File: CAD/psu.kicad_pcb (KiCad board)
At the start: 2 copper layers, 85.5 x 107 mm, 33 parts, among them J2 Vout conn, J3 OLED Pins, J4 GND/-, Q1 tip35c, Q2 BD139, Q3 BC184C, Q4 BC547, T1 220/24, U1 TL431LP, U2 LM317_TO-220, U3 DS18B20

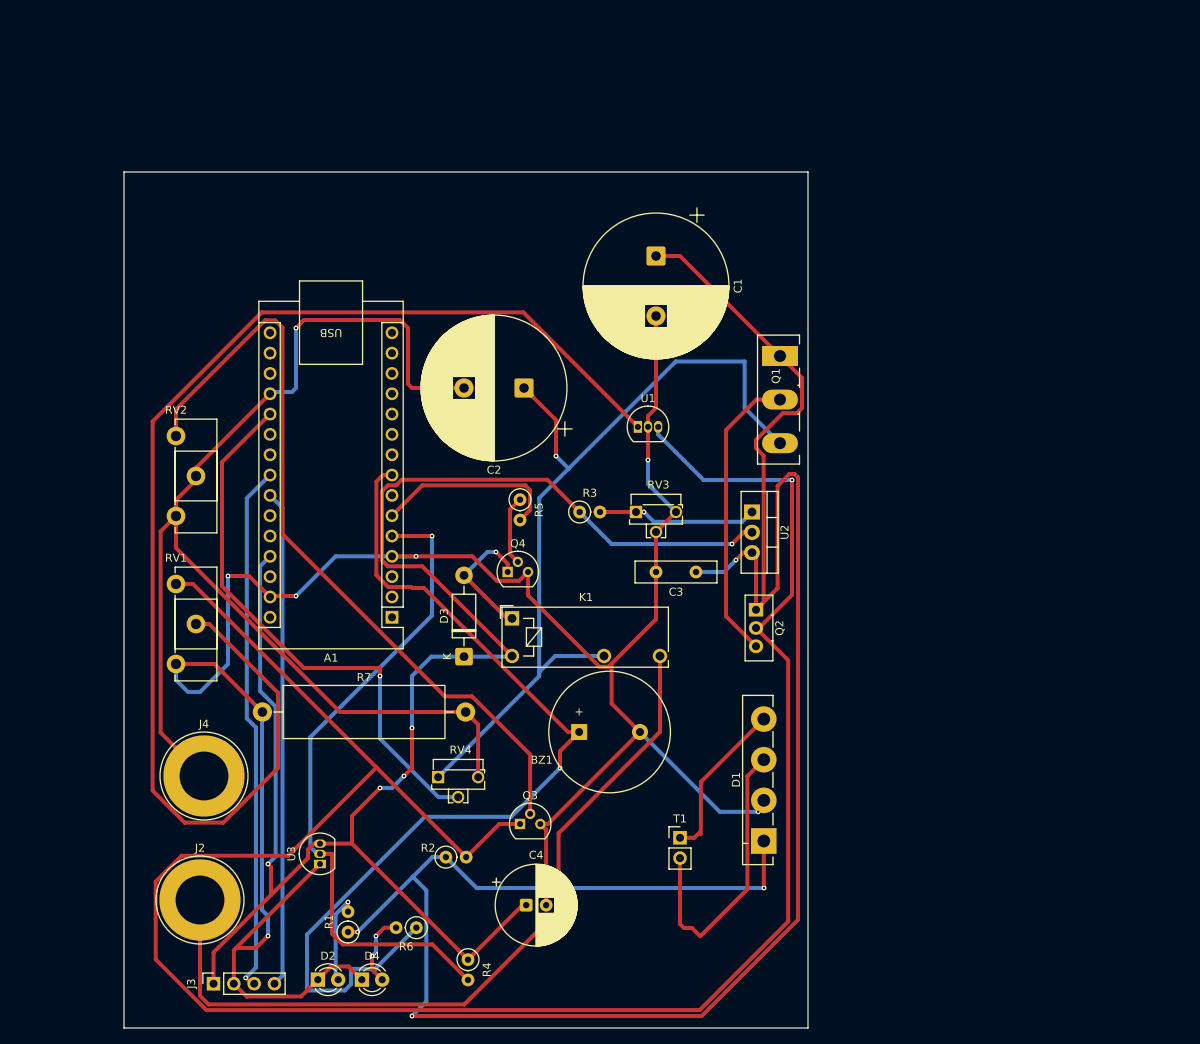
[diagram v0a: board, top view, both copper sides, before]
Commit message: PCB and SCH finished and PDF for self manufacturing finished
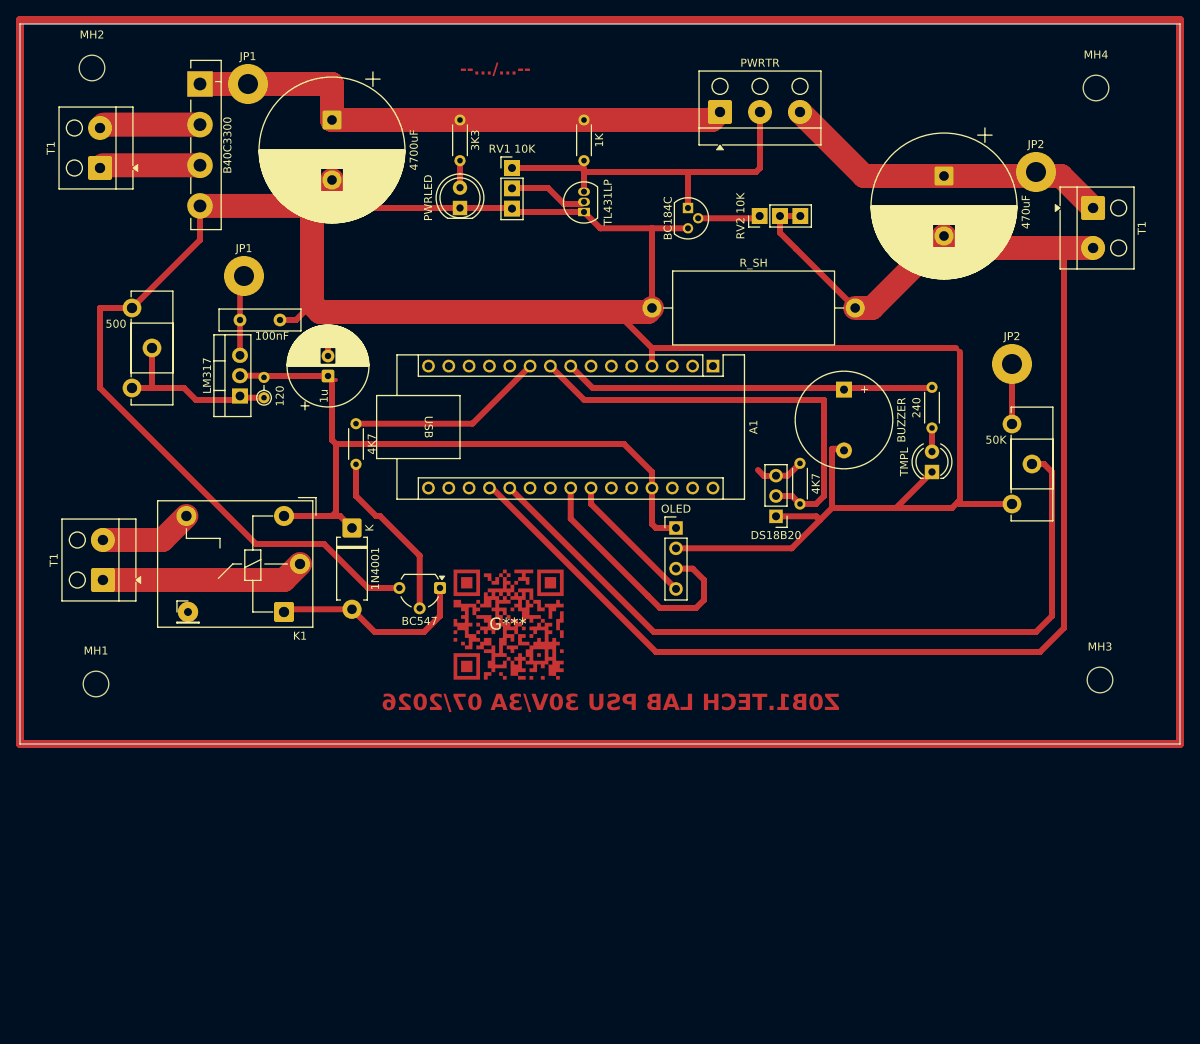
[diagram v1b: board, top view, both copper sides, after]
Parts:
- removed BZ1: T_Buzzer, Buzzer_Beeper:Buzzer_15x7.5RM7.6
- removed C1: 4700uF 40V, Capacitor_THT:CP_Radial_D18.0mm_P7.50mm
- removed C2: 470uF 40v, Capacitor_THT:CP_Radial_D18.0mm_P7.50mm
- removed C3: 100n, Capacitor_THT:C_Disc_D10.0mm_W2.5mm_P5.00mm
- removed C4: 1u, Capacitor_THT:CP_Radial_D10.0mm_P2.50mm
- removed D1: ABS2, Diode_THT:Diode_Bridge_Vishay_GBL
- removed D2: LED, LED_THT:LED_D3.0mm
- removed D3: D, Diode_THT:D_DO-41_SOD81_P10.16mm_Horizontal
- removed D4: T_LED, LED_THT:LED_D3.0mm
- removed J2: Vout conn, Connector:Banana_Jack_1Pin
- removed J3: OLED Pins, Connector_PinSocket_2.54mm:PinSocket_1x04_P2.54mm_Vertical
- removed J4: GND/-, Connector:Banana_Jack_1Pin
- removed Q1: tip35c, Package_TO_SOT_THT:TO-247-3_Vertical
- removed Q2: BD139, Package_TO_SOT_THT:TO-126-3_Vertical
- removed Q3: BC184C, Package_TO_SOT_THT:TO-92
- removed Q4: BC547, Package_TO_SOT_THT:TO-92
- removed R1: 3k3, Resistor_THT:R_Axial_DIN0207_L6.3mm_D2.5mm_P2.54mm_Vertical
- removed R2: 1k, Resistor_THT:R_Axial_DIN0207_L6.3mm_D2.5mm_P2.54mm_Vertical
- removed R3: 120, Resistor_THT:R_Axial_DIN0207_L6.3mm_D2.5mm_P2.54mm_Vertical
- removed R4, R5: 4k7, Resistor_THT:R_Axial_DIN0207_L6.3mm_D2.5mm_P2.54mm_Vertical
- removed R6: 220, Resistor_THT:R_Axial_DIN0207_L6.3mm_D2.5mm_P2.54mm_Vertical
- removed R7: 0R5/5W, Resistor_THT:R_Axial_Power_L20.0mm_W6.4mm_P25.40mm
- removed RV1, RV2: 10k, Potentiometer_THT:Potentiometer_ACP_CA14-H2,5_Horizontal
- removed RV3: 500, Potentiometer_THT:Potentiometer_Runtron_RM-063_Horizontal
- removed RV4: 50K, Potentiometer_THT:Potentiometer_Runtron_RM-063_Horizontal
- removed the T1 at (103.0, 116.7)
- removed U1: TL431LP, Package_TO_SOT_THT:TO-92_Inline
- removed U2: LM317_TO-220, Package_TO_SOT_THT:TO-220-3_Vertical
- removed U3: DS18B20, Package_TO_SOT_THT:TO-92_Inline
- added 100nF: C_Disc_D10.0mm_W2.5mm_P5.00mm, Capacitor_THT:C_Disc_D10.0mm_W2.5mm_P5.00mm, F.Cu at (48.0, 52.0)
- added 120: R_Axial_DIN0204_L3.6mm_D1.6mm_P2.54mm_Vertical, Resistor_THT:R_Axial_DIN0204_L3.6mm_D1.6mm_P2.54mm_Vertical, F.Cu at (51.0, 61.7)
- added 1K: R_Axial_DIN0204_L3.6mm_D1.6mm_P5.08mm_Horizontal, Resistor_THT:R_Axial_DIN0204_L3.6mm_D1.6mm_P5.08mm_Horizontal, F.Cu at (91.0, 27.0)
- added 1N4001: D_DO-15_P10.16mm_Horizontal, Diode_THT:D_DO-15_P10.16mm_Horizontal, F.Cu at (62.0, 78.0)
- added 1u: CP_Radial_D10.0mm_P2.50mm, Capacitor_THT:CP_Radial_D10.0mm_P2.50mm, F.Cu at (59.0, 59.0)
- added 240: R_Axial_DIN0204_L3.6mm_D1.6mm_P5.08mm_Horizontal, Resistor_THT:R_Axial_DIN0204_L3.6mm_D1.6mm_P5.08mm_Horizontal, F.Cu at (134.5, 65.5)
- added 3K3: R_Axial_DIN0204_L3.6mm_D1.6mm_P5.08mm_Horizontal, Resistor_THT:R_Axial_DIN0204_L3.6mm_D1.6mm_P5.08mm_Horizontal, F.Cu at (75.5, 27.0)
- added 4700uF: CP_Radial_D18.0mm_P7.50mm, Capacitor_THT:CP_Radial_D18.0mm_P7.50mm, F.Cu at (59.5, 27.0)
- added 470uF: CP_Radial_D18.0mm_P7.50mm, Capacitor_THT:CP_Radial_D18.0mm_P7.50mm, F.Cu at (136.0, 34.0)
- added 4K7: R_Axial_DIN0204_L3.6mm_D1.6mm_P5.08mm_Horizontal, Resistor_THT:R_Axial_DIN0204_L3.6mm_D1.6mm_P5.08mm_Horizontal, F.Cu at (62.5, 70.0)
- added 4K7: R_Axial_DIN0204_L3.6mm_D1.6mm_P5.08mm_Horizontal, Resistor_THT:R_Axial_DIN0204_L3.6mm_D1.6mm_P5.08mm_Horizontal, F.Cu at (118.0, 75.0)
- added 500: Potentiometer_ACP_CA14-H2,5_Horizontal, Potentiometer_THT:Potentiometer_ACP_CA14-H2,5_Horizontal, F.Cu at (34.5, 50.5)
- added 50K: Potentiometer_ACP_CA14-H2,5_Horizontal, Potentiometer_THT:Potentiometer_ACP_CA14-H2,5_Horizontal, F.Cu at (144.5, 65.0)
- added B40C3300: Diode_Bridge_Vishay_GBL, Diode_THT:Diode_Bridge_Vishay_GBL, F.Cu at (43.0, 22.5)
- added BC184C: TO-92L, Package_TO_SOT_THT:TO-92L, F.Cu at (104.0, 38.0)
- added BC547: TO-92L_Wide, Package_TO_SOT_THT:TO-92L_Wide, F.Cu at (73.0, 85.5)
- added BUZZER: Buzzer_12x9.5RM7.6, Buzzer_Beeper:Buzzer_12x9.5RM7.6, F.Cu at (123.5, 60.7)
- added DS18B20: PinHeader_1x03_P2.54mm_Vertical, Connector_PinHeader_2.54mm:PinHeader_1x03_P2.54mm_Vertical, F.Cu at (115.0, 76.5)
- added G***: LOGO, Serbia:qr, F.Cu at (81.5, 90.0)
- added JP1: MountingHole_2.5mm_Pad, MountingHole:MountingHole_2.5mm_Pad, F.Cu at (49.0, 22.5)
- added JP1: MountingHole_2.5mm_Pad, MountingHole:MountingHole_2.5mm_Pad, F.Cu at (48.5, 46.5)
- added JP2: MountingHole_2.5mm_Pad, MountingHole:MountingHole_2.5mm_Pad, F.Cu at (147.5, 33.5)
- added JP2: MountingHole_2.5mm_Pad, MountingHole:MountingHole_2.5mm_Pad, F.Cu at (144.5, 57.5)
- added LM317: TO-220-3_Vertical, Package_TO_SOT_THT:TO-220-3_Vertical, F.Cu at (48.0, 61.5)
- added MH1: MountingHole_3.2mm_M3, MountingHole:MountingHole_3.2mm_M3, F.Cu at (30.0, 97.5)
- added MH2: MountingHole_3.2mm_M3, MountingHole:MountingHole_3.2mm_M3, F.Cu at (29.5, 20.5)
- added MH3: MountingHole_3.2mm_M3, MountingHole:MountingHole_3.2mm_M3, F.Cu at (155.5, 97.0)
- added MH4: MountingHole_3.2mm_M3, MountingHole:MountingHole_3.2mm_M3, F.Cu at (155.0, 23.0)
- added OLED: PinHeader_1x04_P2.54mm_Vertical, Connector_PinHeader_2.54mm:PinHeader_1x04_P2.54mm_Vertical, F.Cu at (102.5, 78.0)
- added PWRLED: LED_D5.0mm, LED_THT:LED_D5.0mm, F.Cu at (75.5, 38.0)
- added PWRTR: Altech_AK100_1x03_P5.00mm, TerminalBlock_Altech:Altech_AK100_1x03_P5.00mm, F.Cu at (108.0, 26.0)
- added REF**: PinHeader_1x01_P2.54mm_Vertical, Connector_PinHeader_2.54mm:PinHeader_1x01_P2.54mm_Vertical, F.Cu at (41.5, 88.5)
- added RV1 10K: PinHeader_1x03_P2.54mm_Vertical, Connector_PinHeader_2.54mm:PinHeader_1x03_P2.54mm_Vertical, F.Cu at (82.0, 33.0)
- added RV2 10K: PinHeader_1x03_P2.54mm_Vertical, Connector_PinHeader_2.54mm:PinHeader_1x03_P2.54mm_Vertical, F.Cu at (113.0, 39.0)
- added R_SH: R_Axial_DIN0922_L20.0mm_D9.0mm_P25.40mm_Horizontal, Resistor_THT:R_Axial_DIN0922_L20.0mm_D9.0mm_P25.40mm_Horizontal, F.Cu at (99.5, 50.5)
- added T1: VOUT, TerminalBlock_Altech:Altech_AK100_1x02_P5.00mm, F.Cu at (30.9, 84.5)
- added T1: VOUT, TerminalBlock_Altech:Altech_AK100_1x02_P5.00mm, F.Cu at (154.6, 38.0)
- added T1: 220V/24V, TerminalBlock_Altech:Altech_AK100_1x02_P5.00mm, F.Cu at (30.5, 33.0)
- added TL431LP: TO-92L_Inline, Package_TO_SOT_THT:TO-92L_Inline, F.Cu at (91.0, 38.5)
- added TMPL: LED_D4.0mm, LED_THT:LED_D4.0mm, F.Cu at (134.5, 71.0)
- K1: value ~ -> Relay_SPST_Hongfa_JQC-3FF_0XX-1H; footprint Relay_THT:Relay_SPST_Omron_G5NB -> Relay_THT:Relay_SPST_Hongfa_JQC-3FF_0XX-1H
- moved A1 50.9 mm to (107.1, 57.8), turned to -90 degrees
- moved K1 28.5 mm to (53.5, 88.5), turned to 180 degrees
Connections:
- K1 pad 13: Vout -> (no net)
- K1 pad 14: Net-(J2-Pin_1) -> (no net)
- K1 pad A1: Net-(D3-A) -> (no net)
- K1 pad A2: +5V -> (no net)
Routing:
- net (no net): track 0.00 -> 333.6 mm
- net /DCOUT: track 283.8 -> 0.00 mm, vias 4 -> 0
- net Net-(Q2-B): track 267.3 -> 0.00 mm, vias 1 -> 0
- net Net-(U1-REF): track 161.7 -> 0.00 mm
- net +5V: track 220.6 -> 96.8 mm, vias 5 -> 0
- net Vout: track 106.2 -> 0.00 mm, vias 1 -> 0
- net Net-(J2-Pin_1): track 99.2 -> 0.00 mm
- net Net-(Q3-B): track 97.2 -> 0.00 mm
- net Net-(A1-D2): track 81.8 -> 0.00 mm, vias 1 -> 0
- net /DCOUT-: track 275.7 -> 349.5 mm, vias 6 -> 0
- net Net-(A1-D5): track 118.2 -> 46.3 mm, vias 1 -> 0
- net unconnected-(A1-D6-Pad9): track 0.00 -> 54.8 mm
- net Net-(A1-SCL/A5): track 62.1 -> 17.0 mm
- net Net-(Q1-B): track 36.9 -> 0.00 mm
- net Net-(A1-SDA/A4): track 66.4 -> 32.1 mm, vias 1 -> 0
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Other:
- board size 85.5 x 107 mm -> 145 x 90 mm
- board text added: "--.../...--"
- board text added: "Z0B1.TECH LAB PSU 30V/3A 07/2026"

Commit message: Built software for Arduino and added BOM to Readme
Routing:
- net +5V: track 96.8 -> 112.1 mm
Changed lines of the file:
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@@
 	)
 	(segment
-		(start 113.5 71.5)
-		(end 114.96 71.5)
+		(start 99.5 77.5)
+		(end 99.5 73)
+		(width 0.75)
+		(layer "F.Cu")
+		(net "+5V")
+	)
+	(segment
+		(start 100 78)
+		(end 99.5 77.5)
 		(width 0.75)
 		(layer "F.Cu")
@@
 	)
 	(segment
-		(start 102.5 78)
+		(start 109 78)
 		(end 100 78)
 		(width 0.75)
@@
 		(start 59.5 67)
 		(end 59.5 59.5)
+		(width 0.75)
+		(layer "F.Cu")
+		(net "+5V")
+	)
+	(segment
+		(start 114.96 71.5)
+		(end 113.5 71.5)
+		(width 0.75)
+		(layer "F.Cu")
+		(net "+5V")
+	)
+	(segment
+		(start 112.75 70.75)
+		(end 111.5 72)
 		(width 0.75)
 		(layer "F.Cu")
@@
 	)
 	(segment
-		(start 113.5 71.5)
-		(end 112.75 70.75)
-		(width 0.75)
-		(layer "F.Cu")
-		(net "+5V")
-	)
-	(segment
 		(start 62 78)
 		(end 62.75 77.25)
@@
 		(start 62 78)
 		(end 60.5 76.5)
+		(width 0.75)
+		(layer "F.Cu")
+		(net "+5V")
+	)
+	(segment
+		(start 113.5 71.5)
+		(end 112.75 70.75)
 		(width 0.75)
 		(layer "F.Cu")
@@
 	)
 	(segment
-		(start 99.5 77.5)
-		(end 99.5 73)
-		(width 0.75)
-		(layer "F.Cu")
-		(net "+5V")
-	)
-	(segment
 		(start 50.78 58.96)
 		(end 51 59.18)
@@
 	)
 	(segment
-		(start 100 78)
-		(end 99.5 77.5)
+		(start 111.5 72)
+		(end 111.5 75.5)
 		(width 0.75)
 		(layer "F.Cu")
+		(net "+5V")
+	)
+	(segment
+		(start 111.5 75.5)
+		(end 109 78)
+		(width 0.75)
+		(layer "F.Cu")
